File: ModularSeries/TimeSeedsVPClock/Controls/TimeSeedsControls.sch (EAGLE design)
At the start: 19 parts

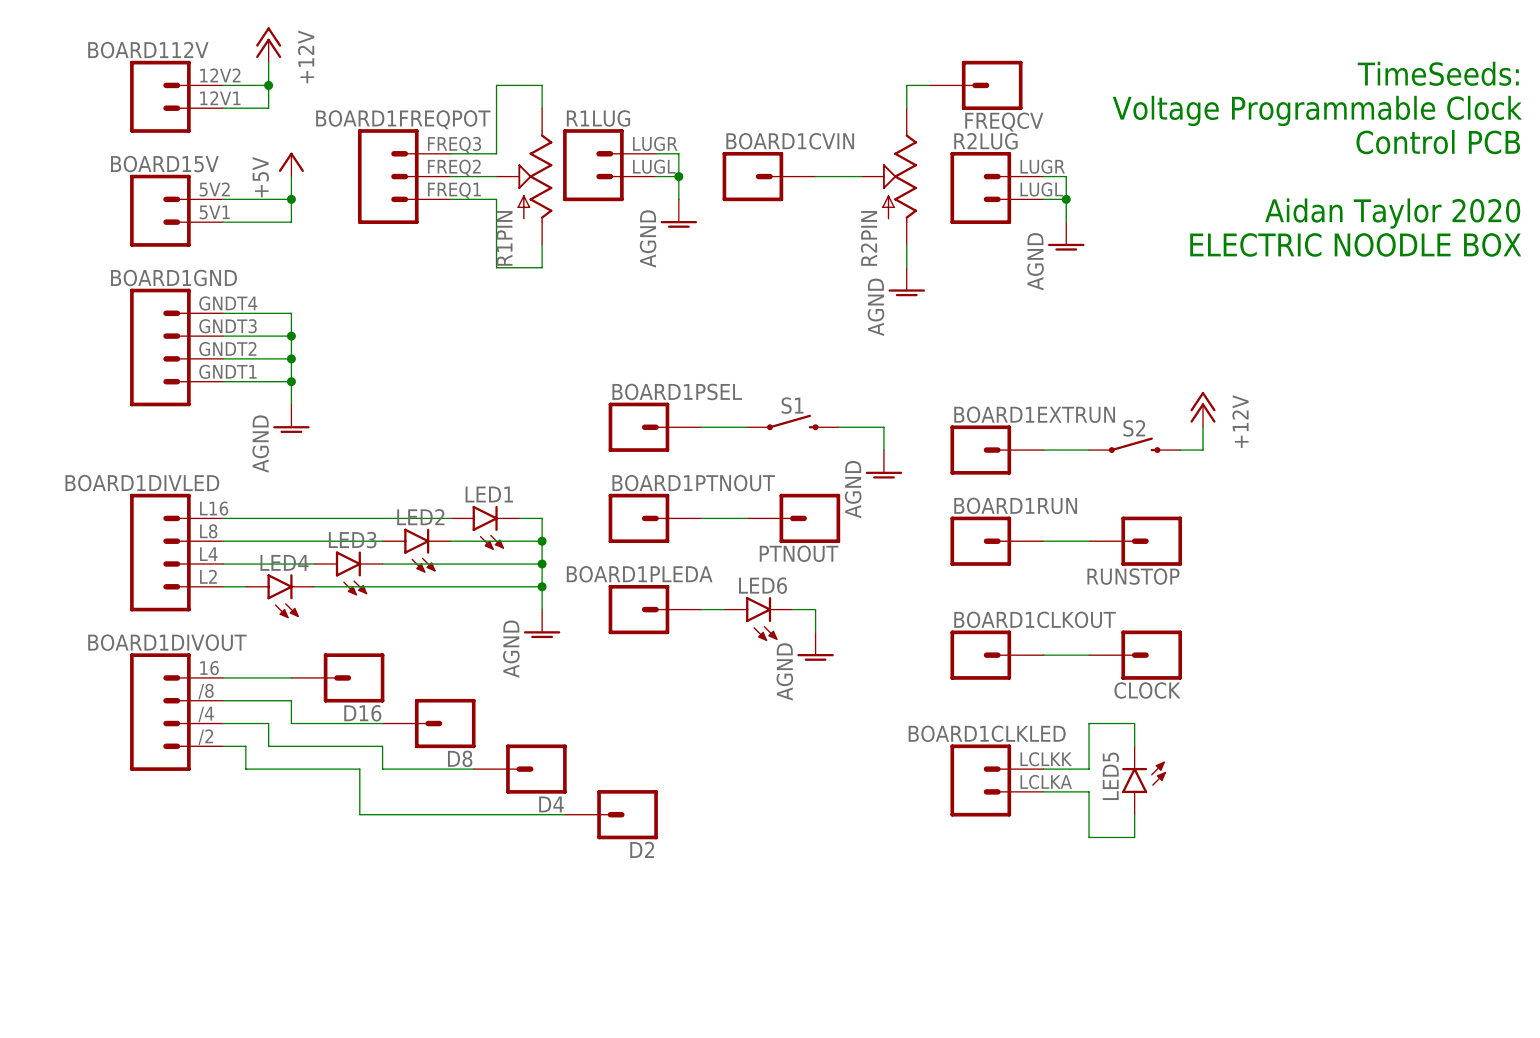
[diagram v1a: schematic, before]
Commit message: Common collector + emitter follower pulse output added to Knives, docs updated
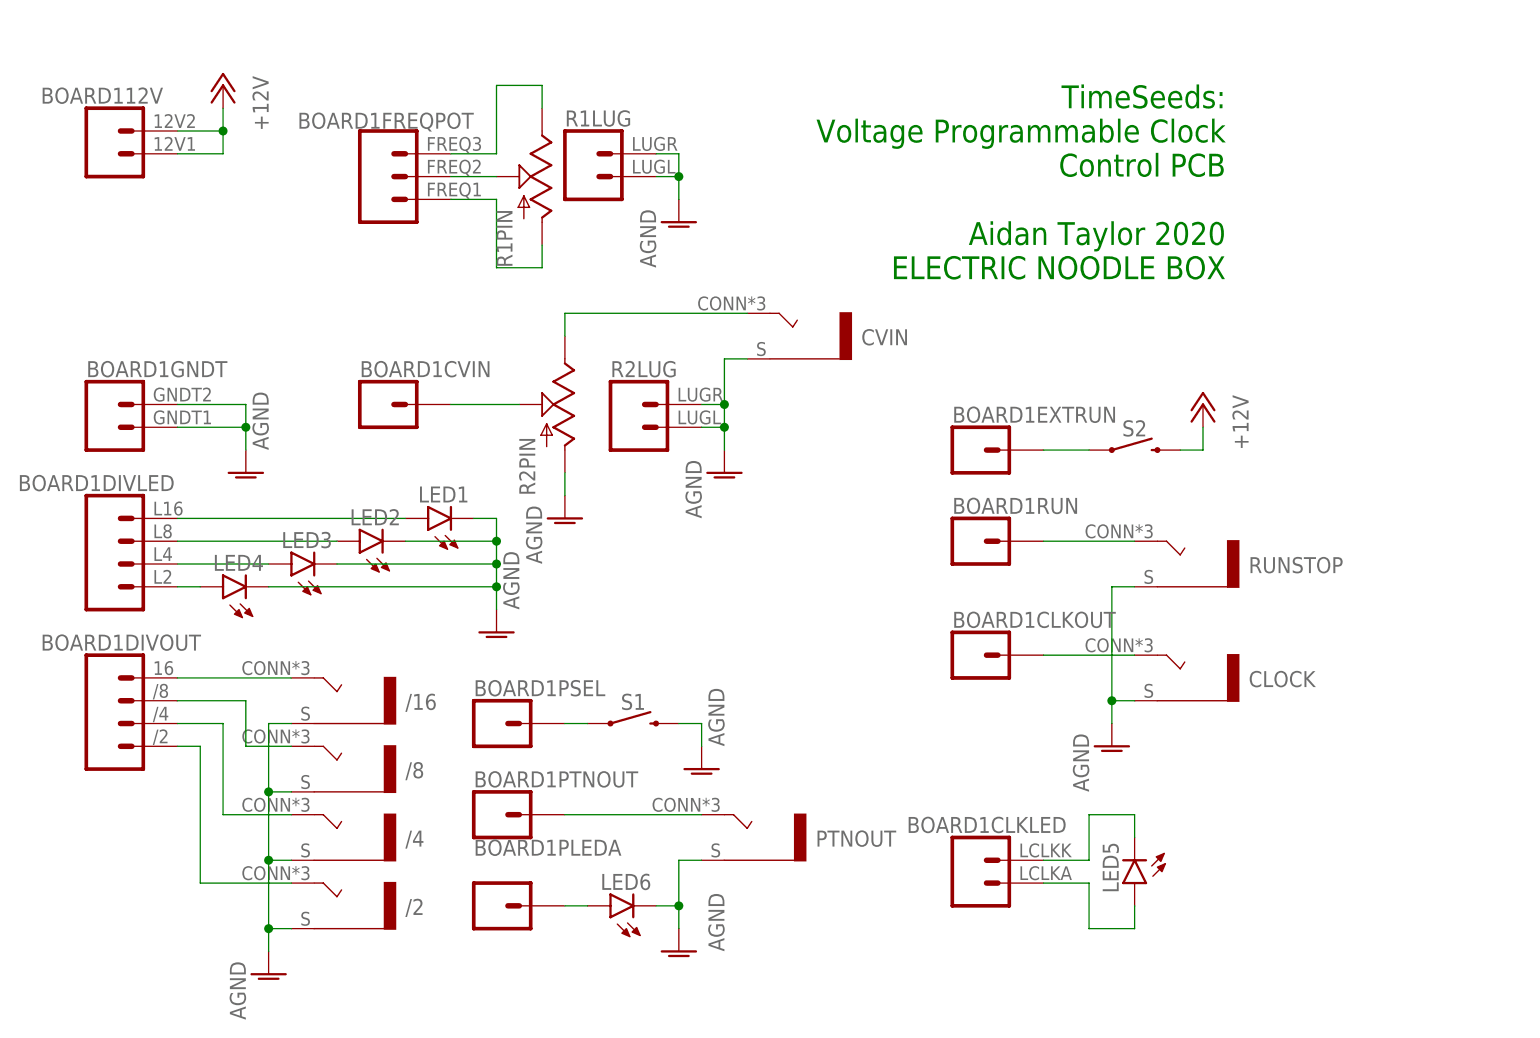
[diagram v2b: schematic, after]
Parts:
- removed D16, D2, D4, D8, FREQCV: BANANA_PANEL, ElectricNoodleBox:BANANA_PANEL
- added /16, /2, /4, /8, CVIN: COMBI-JACKCINCHNANA, ElectricNoodleBox:COMBI-JACKCINCHNANA
- CLOCK, PTNOUT, RUNSTOP: value BANANA_PANEL -> COMBI-JACKCINCHNANA; device ElectricNoodleBox:BANANA_PANEL -> ElectricNoodleBox:COMBI-JACKCINCHNANA
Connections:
- removed net +5V: BOARD15V.1, BOARD15V.2
- net AGND: now also /16.S, /2.S, /4.S, /8.S, BOARD1GNDT.1, BOARD1GNDT.2, CLOCK.S, CVIN.S, PTNOUT.S, RUNSTOP.S; no longer BOARD1GND.1, BOARD1GND.2, BOARD1GND.3, BOARD1GND.4
- net N$16: now also CVIN.T; no longer FREQCV.1
- net N$17: now also PTNOUT.T; no longer PTNOUT.1
- net N$21: now also RUNSTOP.T; no longer RUNSTOP.1
- net N$5: now also /16.T; no longer D16.1
- net N$6: now also /8.T; no longer D8.1
- net N$7: now also /4.T; no longer D4.1
- net N$8: now also /2.T; no longer D2.1
- net N$9: now also CLOCK.T; no longer CLOCK.1
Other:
- moved on the sheet: BOARD112V, BOARD1CLKLED, BOARD1CVIN, BOARD1DIVLED, BOARD1DIVOUT, BOARD1PLEDA, BOARD1PSEL, BOARD1PTNOUT, LED1, LED2, LED3, LED4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
